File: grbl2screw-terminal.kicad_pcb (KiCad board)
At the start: 2 copper layers, 114.3 x 83.8 mm, 28 parts, among them J1 Coolant, J10 Y_motor, J11 Z_motor, J12 Spindle, J2 Start, J3 Pause, J4 Stop, J5 Probe, J6 X_Limit, J7 Y_Limit, J8 Z_Limit, J9 X_Motor

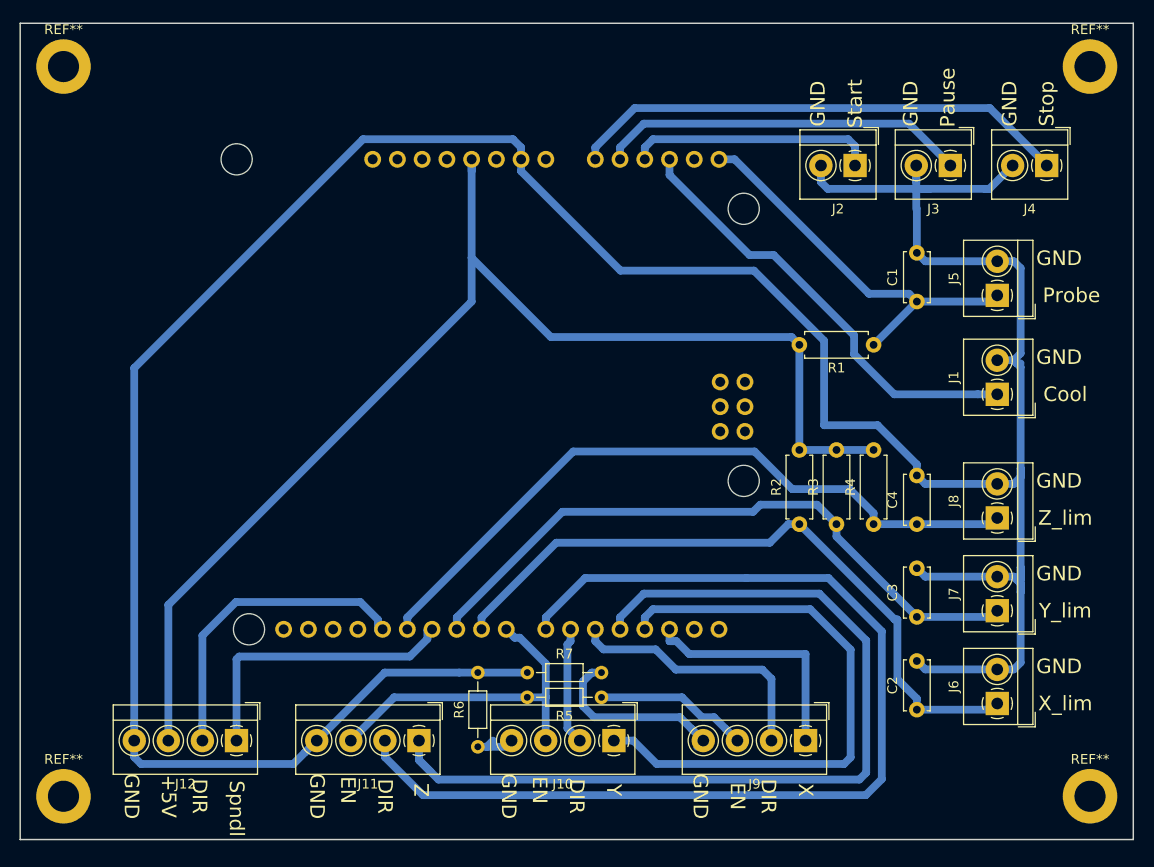
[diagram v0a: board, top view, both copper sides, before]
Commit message: noise protection for the switches
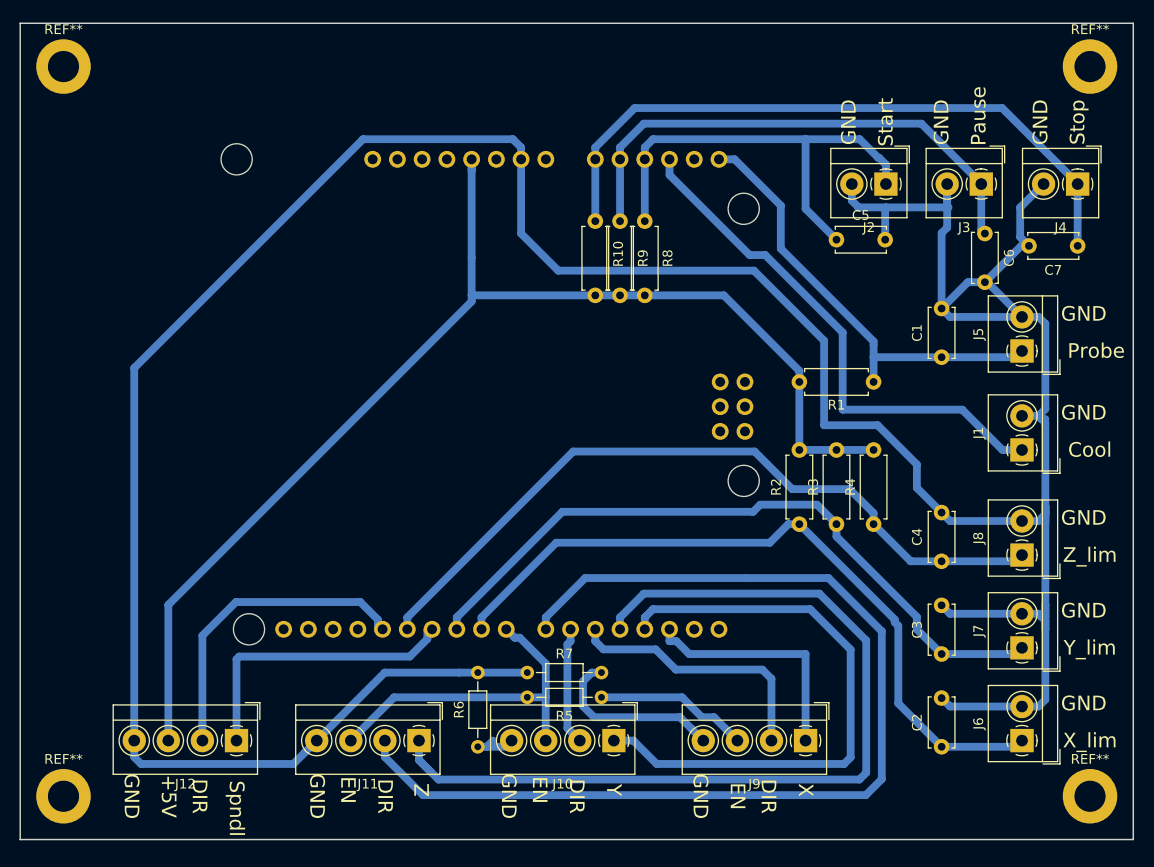
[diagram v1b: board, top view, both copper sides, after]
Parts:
- added C5: 100nf, Capacitor_THT:C_Disc_D5.0mm_W2.5mm_P5.00mm, F.Cu at (172.7, 66.7)
- added C6: 100nf, Capacitor_THT:C_Disc_D5.0mm_W2.5mm_P5.00mm, F.Cu at (188.0, 66.0)
- added C7: 100nf, Capacitor_THT:C_Disc_D5.0mm_W2.5mm_P5.00mm, F.Cu at (197.5, 67.3)
- added R10: 4.7k, Resistor_THT:R_Axial_DIN0207_L6.3mm_D2.5mm_P7.62mm_Horizontal, F.Cu at (148.0, 64.8)
- added R8: 4.7k, Resistor_THT:R_Axial_DIN0207_L6.3mm_D2.5mm_P7.62mm_Horizontal, F.Cu at (153.0, 64.8)
- added R9: 4.7k, Resistor_THT:R_Axial_DIN0207_L6.3mm_D2.5mm_P7.62mm_Horizontal, F.Cu at (150.5, 64.8)
- moved J1 6.25 mm to (191.8, 88.3)
- moved J5 6.25 mm to (191.8, 78.1)
- moved C1 6.25 mm to (183.5, 78.7)
- moved J6 4.58 mm to (191.8, 118.1)
- moved J8 4.58 mm to (191.8, 99.1)
- moved J7 4.58 mm to (191.8, 108.6)
- moved C2 4.58 mm to (183.5, 118.7)
- moved C3 4.58 mm to (183.5, 109.2)
- moved C4 4.58 mm to (183.5, 99.7)
- moved R1 3.81 mm to (176.5, 81.3)
- moved J2 3.70 mm to (177.8, 61.0)
- moved J3 3.70 mm to (187.6, 61.0)
- moved J4 3.70 mm to (197.5, 61.0)
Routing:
- net GNDREF: track 323.2 -> 352.2 mm
- net Net-(C5-Pad1): track 25.4 -> 47.4 mm
- net Net-(C7-Pad1): track 51.7 -> 68.4 mm
- net Net-(C6-Pad1): track 38.0 -> 53.5 mm
- net Net-(J1-Pad1): track 45.7 -> 54.1 mm
- net Net-(C3-Pad1): track 67.3 -> 72.2 mm
- net Net-(C1-Pad1): track 41.2 -> 45.9 mm
- net Net-(C2-Pad1): track 70.6 -> 75.3 mm
- net Net-(C4-Pad1): track 72.9 -> 77.0 mm
- net Net-(J12-Pad3): track 129.6 -> 126.4 mm
